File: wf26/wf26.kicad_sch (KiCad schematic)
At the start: 7 parts, among them J1 WF26 -> TV20 S bus, K1 HJR-4102-N-12V

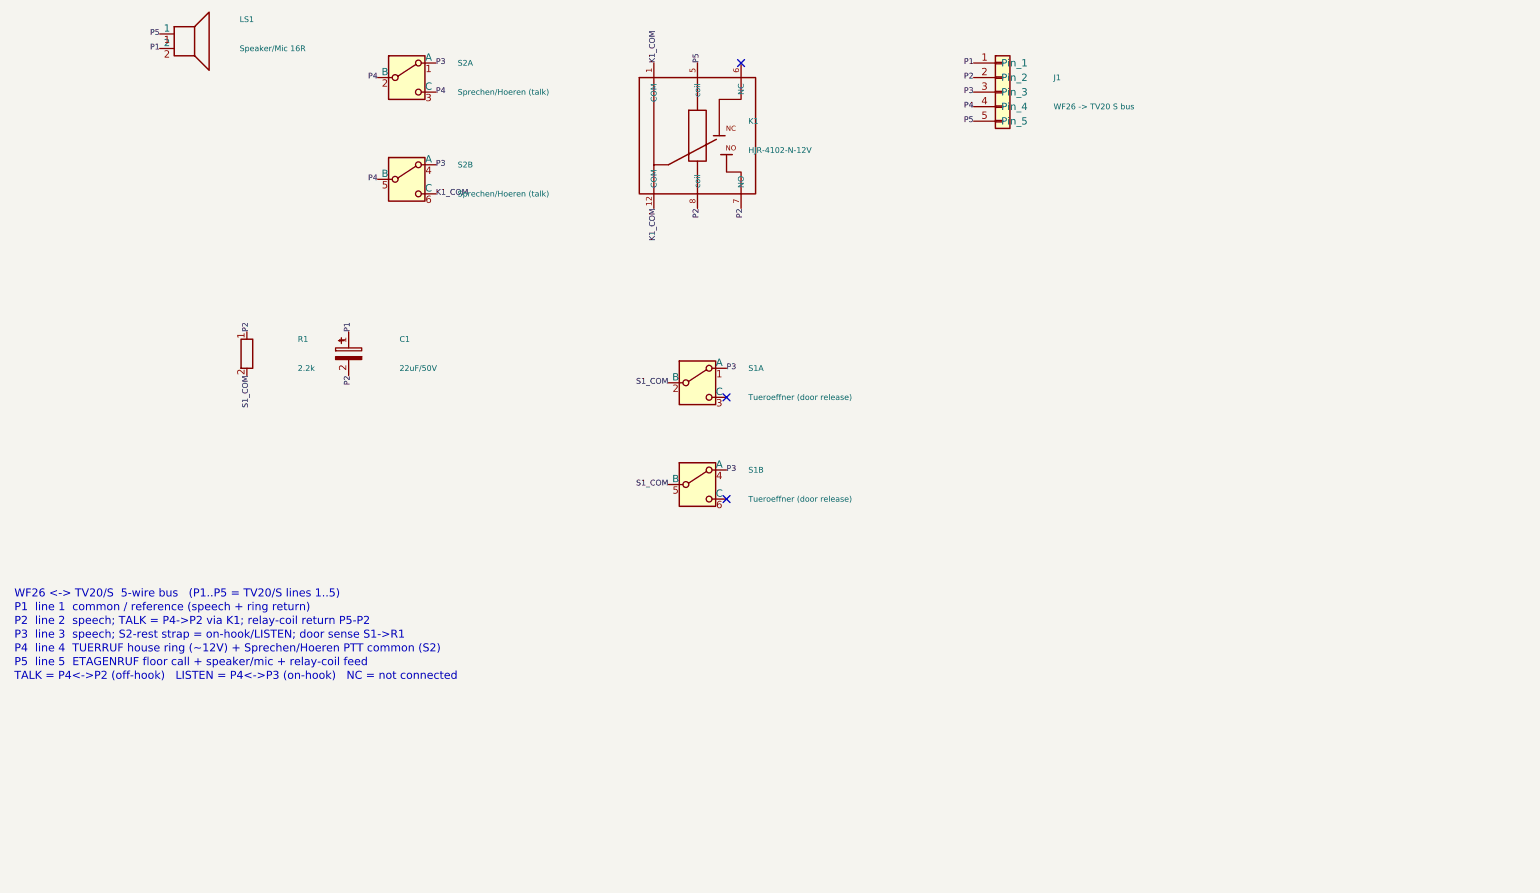
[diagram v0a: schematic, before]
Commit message: WF26: wire the internal schematic, assign THT footprints, fix DPDT pad map
- wf26.kicad_sch: rebuilt as a fully-wired 5-rail bus (P1-P5) with real
  inter-component wiring and junctions; THT footprints on every part
- Corrected S1/S2 pole-1 throws (footprint pads 1<->3) to match the real
  C&K DPDT (both poles' P3 throws on the same physical side)
- DESIGN.md: WF26 internal-netlist table updated to match
- Added wire_wf26.py generator plus WF26 reference material (pinout notes,
  TV20S photo) and an initial wf26.kicad_pcb
- gitignore KiCad *.lck lock files
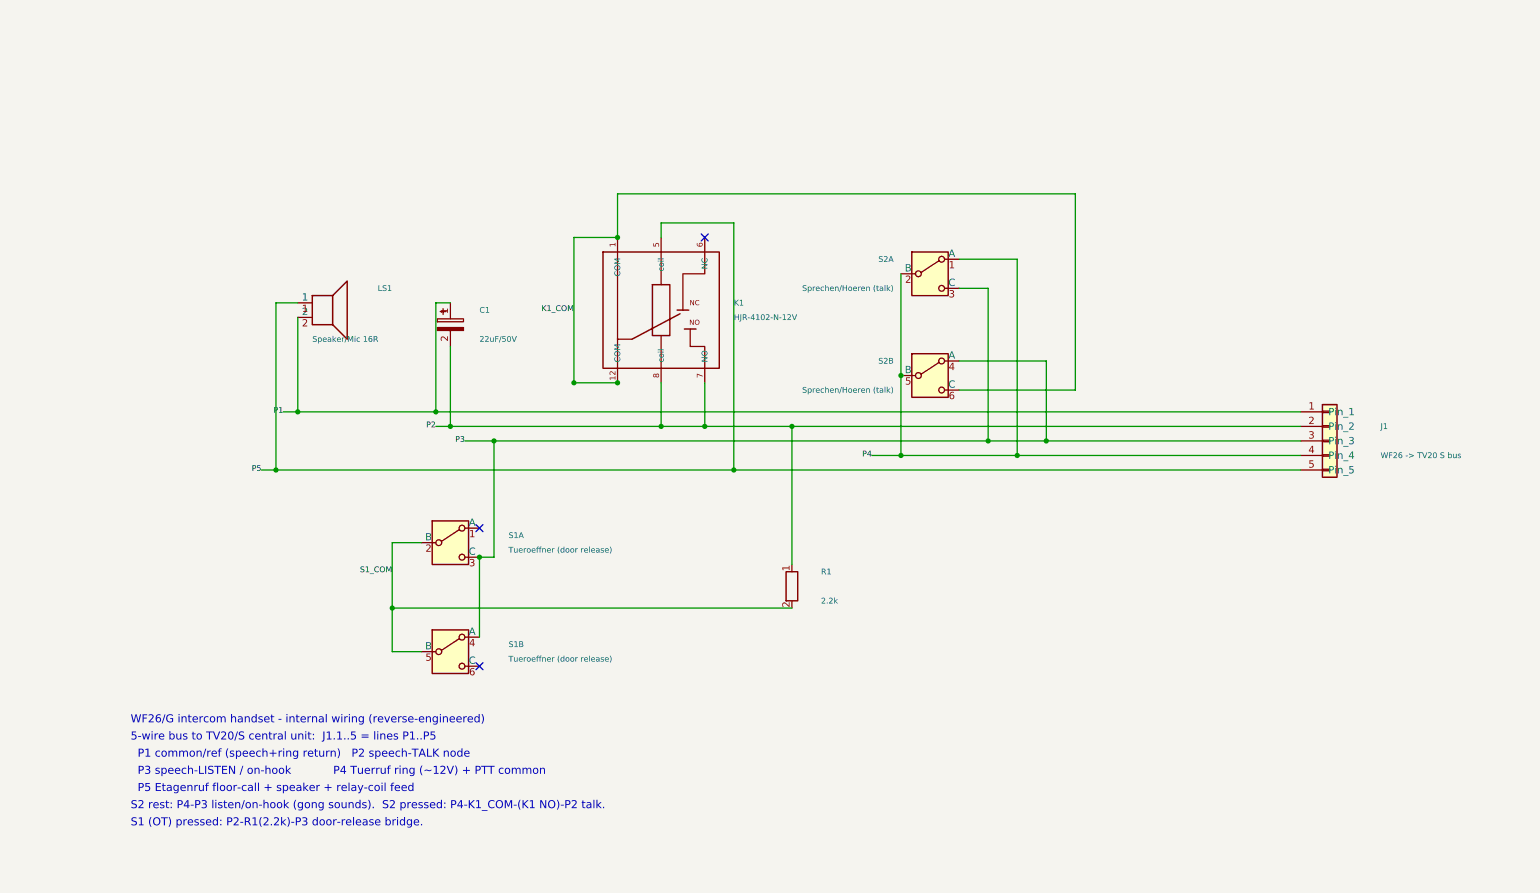
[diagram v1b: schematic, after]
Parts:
- C1: footprint (none) -> Capacitor_THT:CP_Radial_D5.0mm_P2.00mm; now in the parts list
- J1: footprint (none) -> TerminalBlock_Phoenix:TerminalBlock_Phoenix_PT-1,5-5-3.5-H_1x05_P3.50mm_Horizontal; now in the parts list
- K1: footprint (none) -> Relay_THT:Relay_SPDT_HJR-4102; now in the parts list
- LS1: footprint (none) -> Connector_PinHeader_2.54mm:PinHeader_1x02_P2.54mm_Vertical; now in the parts list
- R1: footprint (none) -> Resistor_THT:R_Axial_DIN0207_L6.3mm_D2.5mm_P7.62mm_Horizontal; now in the parts list
- S1, S2: footprint (none) -> Button_Switch_THT:SW_CK_JS202011CQN_DPDT_Straight; now in the parts list
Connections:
- net P3: now also S1.3 (C), S2.3 (C); no longer S1.1 (A), S2.1 (A)
- net P4: now also S2.1 (A); no longer S2.3 (C)
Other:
- note added: "5-wire bus to TV20/S central unit: J1.1..5 = lines P1..P5"
- note added: "P1 common/ref (speech+ring return) P2 speech-TALK node"
- note added: "P3 speech-LISTEN / on-hook P4 Tuerruf ring (~12V) + PTT common"
- note added: "P5 Etagenruf floor-call + speaker + relay-coil feed"
- note added: "S1 (OT) pressed: P2-R1(2.2k)-P3 door-release bridge."
- note added: "S2 rest: P4-P3 listen/on-hook (gong sounds). S2 pressed: P4-K1_COM-(K1 NO)-P2 talk."
- note added: "WF26/G intercom handset - internal wiring (reverse-engineered)"
- note removed: "P1 line 1 common / reference (speech + ring return)"
- note removed: "P2 line 2 speech; TALK = P4->P2 via K1; relay-coil return P5-P2"
- note removed: "P3 line 3 speech; S2-rest strap = on-hook/LISTEN; door sense S1->R1"
- note removed: "P4 line 4 TUERRUF house ring (~12V) + Sprechen/Hoeren PTT common (S2)"
- note removed: "P5 line 5 ETAGENRUF floor call + speaker/mic + relay-coil feed"
- note removed: "TALK = P4<->P2 (off-hook) LISTEN = P4<->P3 (on-hook) NC = not connected"
- note removed: "WF26 <-> TV20/S 5-wire bus (P1..P5 = TV20/S lines 1..5)"
- moved on the sheet: C1, J1, K1, LS1, R1, S1A, S1B, S2A, S2B

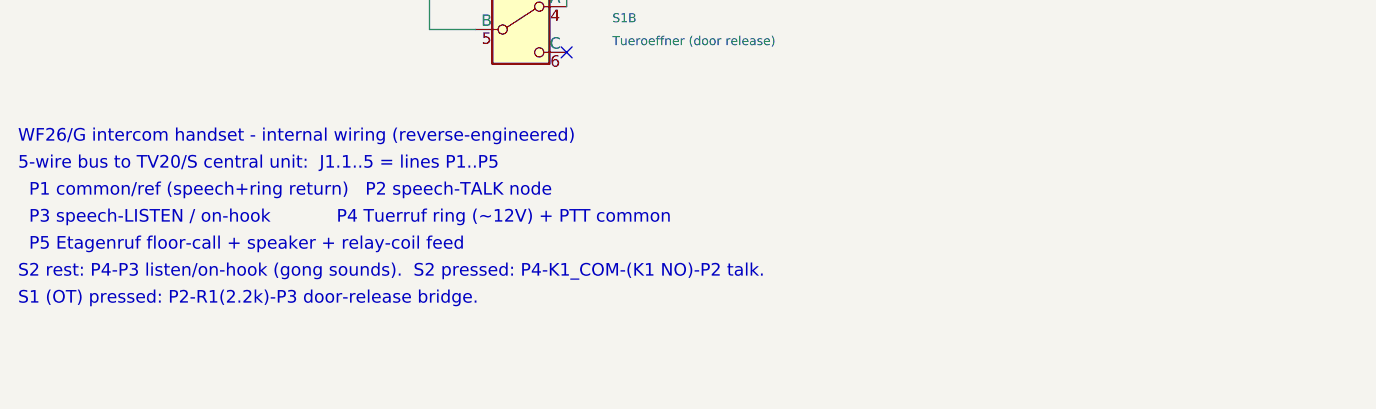
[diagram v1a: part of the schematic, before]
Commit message: WF26: correct talk/listen model (talk = P4↔P3); P2/P3 = door-opener only
Bench measurement: pressing Sprechen shorts P3↔P4, inverting the earlier
(inferred) model. Propagated through the schematic comments and DESIGN.md:

- talk = P4↔P3 (S2 pressed, direct contact); listen = P4↔P2 via the internal
  relay K1 during a session, else P4 floats
- P2/P3 carry no speech — that pair is solely the door-opener (ÖT) buzzer
  trigger; speech/tones are entirely on P1/P5 (LS1, the sole transducer)
- V4 reality: virtual-PTT relay K1 ties IN_P4↔P2 (the listen leg), but talk is
  line 4↔line 3 and P3 is reachable only via the door-opener relay, so
  board-initiated talk is unavailable; fix is K1 NO P2→P3 on a respin, else the
  physical button. Receive/local-playback/senses/door/chime are unaffected
- corrected the relay interlock + release-sequencing rationale and the
  chime-suppression mechanism (breaks line 4 to block the Türruf trigger)
- docs cleanup: full net names (P4 not 4); removed the now-resolved
  P1/P5-vs-2/3 reconciliation open item
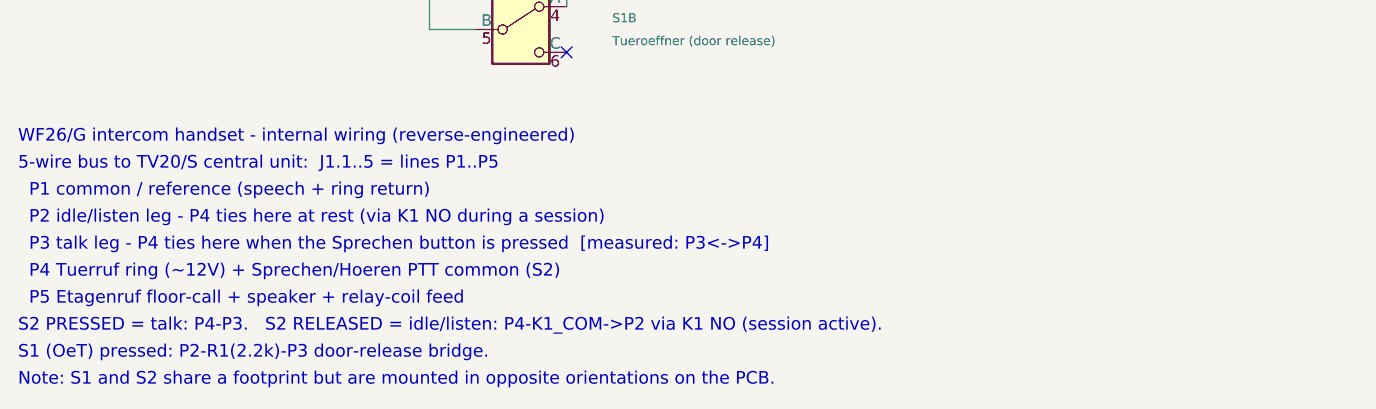
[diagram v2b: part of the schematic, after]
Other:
- note added: "Note: S1 and S2 share a footprint but are mounted in opposite orientations on the PCB."
- note added: "P1 common / reference (speech + ring return)"
- note added: "P2 idle/listen leg - P4 ties here at rest (via K1 NO during a session)"
- note added: "P3 talk leg - P4 ties here when the Sprechen button is pressed [measured: P3<->P4]"
- note added: "P4 Tuerruf ring (~12V) + Sprechen/Hoeren PTT common (S2)"
- note added: "S1 (OeT) pressed: P2-R1(2.2k)-P3 door-release bridge."
- note added: "S2 PRESSED = talk: P4-P3. S2 RELEASED = idle/listen: P4-K1_COM->P2 via K1 NO (session active)."
- note removed: "P1 common/ref (speech+ring return) P2 speech-TALK node"
- note removed: "P3 speech-LISTEN / on-hook P4 Tuerruf ring (~12V) + PTT common"
- note removed: "S1 (OT) pressed: P2-R1(2.2k)-P3 door-release bridge."
- note removed: "S2 rest: P4-P3 listen/on-hook (gong sounds). S2 pressed: P4-K1_COM-(K1 NO)-P2 talk."
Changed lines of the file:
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@@
     (effects (font (size 1.4 1.4)) (justify left))
   )
-  (text "  P1 common/ref (speech+ring return)   P2 speech-TALK node"
-    (at 40.64 164.0 0)
+  (text "  P1 common / reference (speech + ring return)" (at 40.64 164.0 0)
     (effects (font (size 1.4 1.4)) (justify left))
   )
-  (text "  P3 speech-LISTEN / on-hook            P4 Tuerruf ring (~12V) + PTT common"
+  (text "  P2 idle/listen leg - P4 ties here at rest (via K1 NO during a session)"
     (at 40.64 167.0 0)
     (effects (font (size 1.4 1.4)) (justify left))
   )
-  (text "  P5 Etagenruf floor-call + speaker + relay-coil feed"
+  (text "  P3 talk leg - P4 ties here when the Sprechen button is pressed  [measured: P3<->P4]"
     (at 40.64 170.0 0)
     (effects (font (size 1.4 1.4)) (justify left))
   )
-  (text "S2 rest: P4-P3 listen/on-hook (gong sounds).  S2 pressed: P4-K1_COM-(K1 NO)-P2 talk."
+  (text "  P4 Tuerruf ring (~12V) + Sprechen/Hoeren PTT common (S2)"
     (at 40.64 173.0 0)
     (effects (font (size 1.4 1.4)) (justify left))
   )
-  (text "S1 (OT) pressed: P2-R1(2.2k)-P3 door-release bridge."
+  (text "  P5 Etagenruf floor-call + speaker + relay-coil feed"
     (at 40.64 176.0 0)
     (effects (font (size 1.4 1.4)) (justify left))
   )
+  (text "S2 PRESSED = talk: P4-P3.   S2 RELEASED = idle/listen: P4-K1_COM->P2 via K1 NO (session active)."
+    (at 40.64 179.0 0)
+    (effects (font (size 1.4 1.4)) (justify left))
+  )
+  (text "S1 (OeT) pressed: P2-R1(2.2k)-P3 door-release bridge."
+    (at 40.64 182.0 0)
+    (effects (font (size 1.4 1.4)) (justify left))
+  )
+  (text "Note: S1 and S2 share a footprint but are mounted in opposite orientations on the PCB."
+    (at 40.64 185.0 0)
+    (effects (font (size 1.4 1.4)) (justify left))
+  )

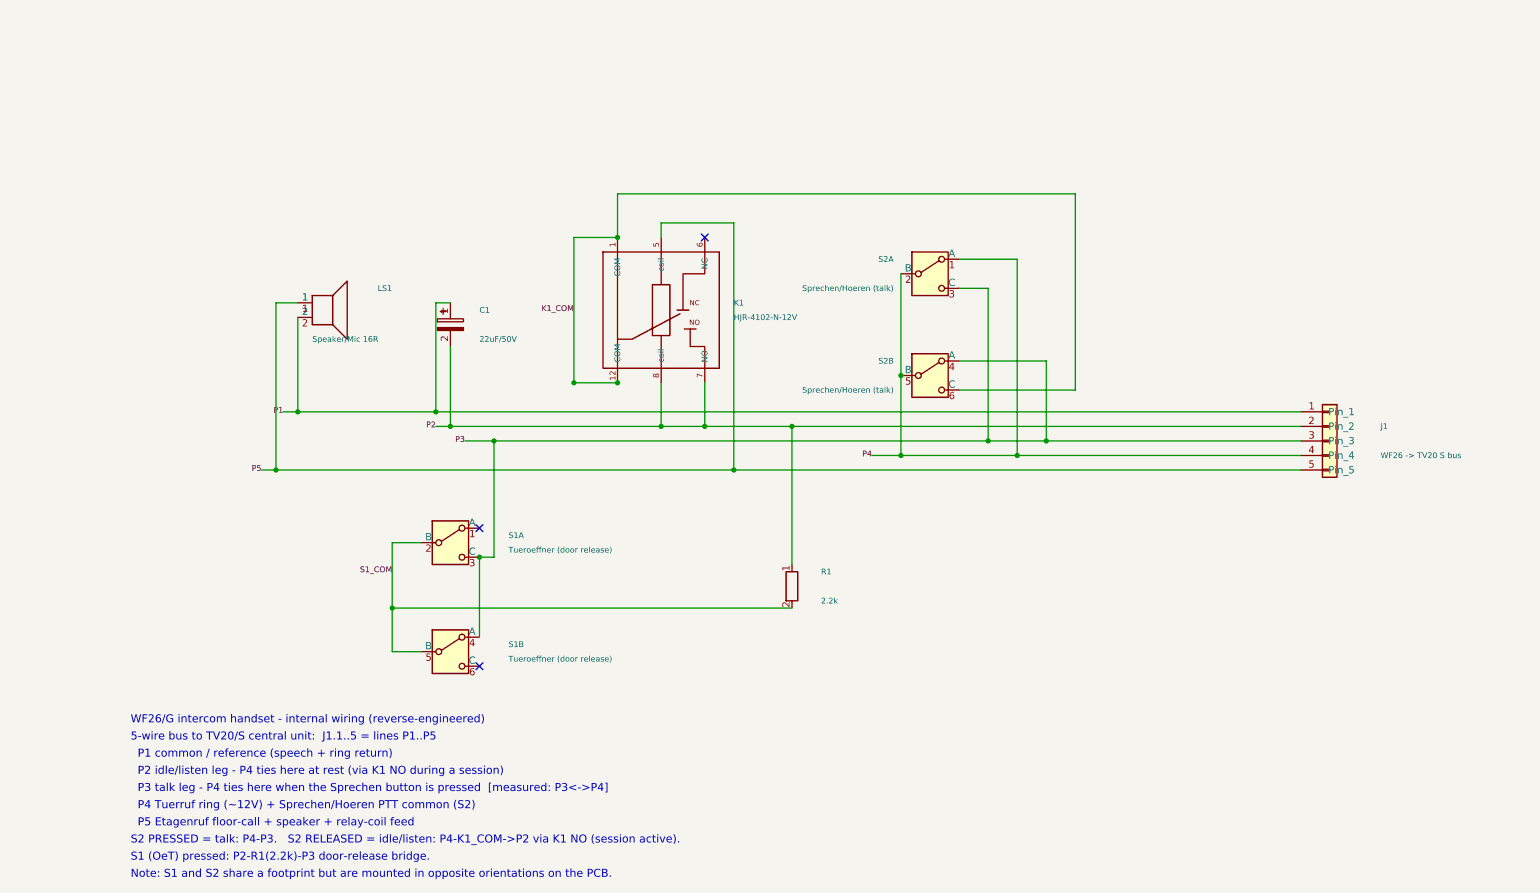
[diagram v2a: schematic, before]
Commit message: WF26: correct relay symbol pinout (pin 6 = NO) and reconcile docs/notes
Confirmed via datasheet + in-circuit continuity that the WF26 internal
relay's P2 sits on the normally-open contact = HJR-4102 pin 6 (the symbol
had NO/NC swapped):
- sym/wf26.kicad_sym: pin 6 = NO, pin 7 = NC; pins reordered to a
  consistent top-view layout (1/12 and 5/8 swaps are no-ops: COM tied,
  coil symmetric)
- schematic notes: talk/listen via WF26_K1 NO; refdes K1 -> WF26_K1;
  line 5/P5 reaches the bus via the external Etagenruf (ET) button
- DESIGN.md: relay pinout, refdes (WF26_K1 / K1_COM / OT_BRIDGE), speech
  on bus pair 2/3 coupled into LS1 via C1, Mithoersperre, talk=P4<->P3 /
  listen=P4<->P2; closed the NO/NC open item

Schematic relay net rewiring (P2 -> pin 6) + Update-from-Library still to
be applied in KiCad.
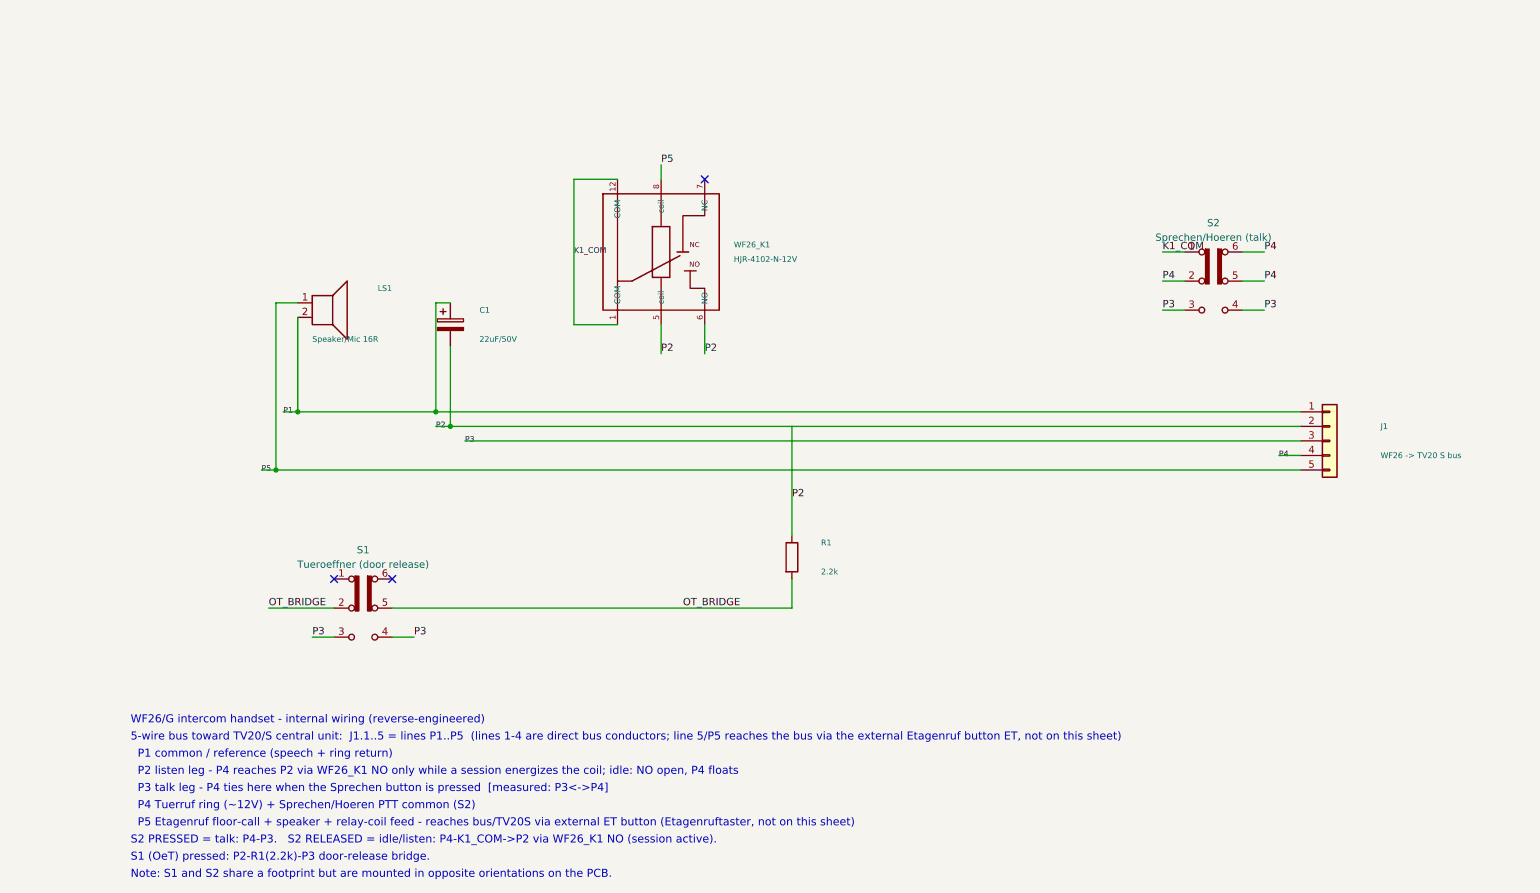
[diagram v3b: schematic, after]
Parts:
- removed S1: Tueroeffner (door release), Button_Switch_THT:SW_CK_JS202011CQN_DPDT_Straight, symbol Switch:SW_DPDT_x2
- removed S2: Sprechen/Hoeren (talk), Button_Switch_THT:SW_CK_JS202011CQN_DPDT_Straight, symbol Switch:SW_DPDT_x2
- added S1: Tueroeffner (door release), Button_Switch_THT:SW_CK_JS202011CQN_DPDT_Straight, symbol Switch:SW_Slide_DPDT
- added S2: Sprechen/Hoeren (talk), Button_Switch_THT:SW_CK_JS202011CQN_DPDT_Straight, symbol Switch:SW_Slide_DPDT
- renumbered K1 to WF26_K1
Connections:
- net K1_COM: now also S2.1 (A)
- net P2: now also WF26_K1.5 (coil), WF26_K1.6 (NO); no longer WF26_K1.7 (NO), WF26_K1.8 (coil)
- net P3: now also S1.3 (C), S1.4 (A), S2.3 (C), S2.4 (A)
- net P4: now also S2.2 (B), S2.5 (B), S2.6 (C)
- net P5: now also WF26_K1.8 (coil); no longer WF26_K1.5 (coil)
- net S1_COM renamed OT_BRIDGE
- net OT_BRIDGE: now also S1.2 (B), S1.5 (B)
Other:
- note added: "5-wire bus toward TV20/S central unit: J1.1..5 = lines P1..P5 (lines 1-4 are direct bus conductors; line 5/P5 reaches the bus via the external Etagenruf button ET, not on this sheet)"
- note added: "P2 listen leg - P4 reaches P2 via WF26_K1 NO only while a session energizes the coil; idle: NO open, P4 floats"
- note added: "P5 Etagenruf floor-call + speaker + relay-coil feed - reaches bus/TV20S via external ET button (Etagenruftaster, not on this sheet)"
- note added: "S2 PRESSED = talk: P4-P3. S2 RELEASED = idle/listen: P4-K1_COM->P2 via WF26_K1 NO (session active)."
- note removed: "5-wire bus to TV20/S central unit: J1.1..5 = lines P1..P5"
- note removed: "P2 idle/listen leg - P4 ties here at rest (via K1 NO during a session)"
- note removed: "P5 Etagenruf floor-call + speaker + relay-coil feed"
- note removed: "S2 PRESSED = talk: P4-P3. S2 RELEASED = idle/listen: P4-K1_COM->P2 via K1 NO (session active)."
- moved on the sheet: WF26_K1
